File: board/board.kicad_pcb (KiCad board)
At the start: 2 copper layers, 31 parts, among them J1 Screw_Terminal_01x02, J2 Screw_Terminal_01x02, Q1 NPN, Q2 NPN, Q3 NPN

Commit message: Updates PCB file
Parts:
- added J3: Screw_Terminal_01x02, TerminalBlock_4Ucon:TerminalBlock_4Ucon_1x02_P3.50mm_Horizontal, F.Cu at (138.7, 132.1)
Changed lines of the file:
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@@
   (net 16 "Net-(Q2-E)")
   (net 17 "Net-(Q3-C)")
+  (footprint "TerminalBlock_4Ucon:TerminalBlock_4Ucon_1x02_P3.50mm_Horizontal" (layer "F.Cu")
+    (at 138.74 132.08)
+    (descr "Terminal Block 4Ucon ItemNo. 19963, 2 pins, pitch 3.5mm, size 7.7x7mm^2, drill diamater 1.2mm, pad diameter 2.4mm, see http://www.4uconnector.com/online/object/4udrawing/19963.pdf, script-generated using https://github.com/pointhi/kicad-footprint-generator/scripts/TerminalBlock_4Ucon")
+    (tags "THT Terminal Block 4Ucon ItemNo. 19963 pitch 3.5mm size 7.7x7mm^2 drill 1.2mm pad 2.4mm")
+    (property "Sheetfile" "board.kicad_sch")
+    (property "Sheetname" "")
+    (property "ki_description" "Generic screw terminal, single row, 01x02, script generated (kicad-library-utils/schlib/autogen/connector/)")
+    (property "ki_keywords" "screw terminal")
+    (attr through_hole)
+    (fp_text reference "J3" (at 1.75 -4.46) (layer "F.SilkS")
+        (effects (font (size 1 1) (thickness 0.15)))
+    )
+    (fp_text value "Screw_Terminal_01x02" (at 1.75 4.66) (layer "F.Fab")
+        (effects (font (size 1 1) (thickness 0.15)))
+    )
+    (fp_text user "${REFERENCE}" (at 1.75 2.9) (layer "F.Fab")
+        (effects (font (size 1 1) (thickness 0.15)))
+    )
+    (fp_line (start -2.4 2.16) (end -2.4 3.9)
+      (stroke (width 0.12) (type solid)) (layer "F.SilkS"))
+    (fp_line (start -2.4 3.9) (end -0.9 3.9)
+      (stroke (width 0.12) (type solid)) (layer "F.SilkS"))
+    (fp_line (start -2.16 -3.46) (end -2.16 3.66)
+      (stroke (width 0.12) (type solid)) (layer "F.SilkS"))
+    (fp_line (start -2.16 -3.46) (end 5.66 -3.46)
+      (stroke (width 0.12) (type solid)) (layer "F.SilkS"))
+    (fp_line (start -2.16 2.1) (end 5.66 2.1)
+      (stroke (width 0.12) (type solid)) (layer "F.SilkS"))
+    (fp_line (start -2.16 3.66) (end 5.66 3.66)
+      (stroke (width 0.12) (type solid)) (layer "F.SilkS"))
+    (fp_line (start 5.66 -3.46) (end 5.66 3.66)
+      (stroke (width 0.12) (type solid)) (layer "F.SilkS"))
+    (fp_arc (start -1.432109 0.607742) (mid -1.555727 -0.00014) (end -1.432 -0.608)
+      (stroke (width 0.12) (type solid)) (layer "F.SilkS"))
+    (fp_arc (start -0.607742 -1.432109) (mid 0.00014 -1.555727) (end 0.608 -1.432)
+      (stroke (width 0.12) (type solid)) (layer "F.SilkS"))
+    (fp_arc (start 0.027011 1.555493) (mid -0.296984 1.527118) (end -0.608 1.432)
+      (stroke (width 0.12) (type solid)) (layer "F.SilkS"))
+    (fp_arc (start 0.607587 1.431385) (mid 0.310017 1.523783) (end 0 1.555)
+      (stroke (width 0.12) (type solid)) (layer "F.SilkS"))
+    (fp_arc (start 1.432109 -0.607742) (mid 1.555727 0.00014) (end 1.432 0.608)
+      (stroke (width 0.12) (type solid)) (layer "F.SilkS"))
+    (fp_circle (center 3.5 0) (end 5.055 0)
+      (stroke (width 0.12) (type solid)) (fill none) (layer "F.SilkS"))
+    (fp_line (start -2.6 -3.9) (end -2.6 4.1)
+      (stroke (width 0.05) (type solid)) (layer "F.CrtYd"))
+    (fp_line (start -2.6 4.1) (end 6.1 4.1)
+      (stroke (width 0.05) (type solid)) (layer "F.CrtYd"))
+    (fp_line (start 6.1 -3.9) (end -2.6 -3.9)
+      (stroke (width 0.05) (type solid)) (layer "F.CrtYd"))
+    (fp_line (start 6.1 4.1) (end 6.1 -3.9)
+      (stroke (width 0.05) (type solid)) (layer "F.CrtYd"))
+    (fp_line (start -2.1 -3.4) (end 5.6 -3.4)
+      (stroke (width 0.1) (type solid)) (layer "F.Fab"))
+    (fp_line (start -2.1 2.1) (end -2.1 -3.4)
+      (stroke (width 0.1) (type solid)) (layer "F.Fab"))
+    (fp_line (start -2.1 2.1) (end 5.6 2.1)
+      (stroke (width 0.1) (type solid)) (layer "F.Fab"))
+    (fp_line (start -1.1 -0.069) (end -0.069 -0.069)
+      (stroke (width 0.1) (type solid)) (layer "F.Fab"))
+    (fp_line (start -1.1 0.069) (end -1.1 -0.069)
+      (stroke (width 0.1) (type solid)) (layer "F.Fab"))
+    (fp_line (start -0.6 3.6) (end -2.1 2.1)
+      (stroke (width 0.1) (type solid)) (layer "F.Fab"))
+    (fp_line (start -0.069 -1.1) (end 0.069 -1.1)
+      (stroke (width 0.1) (type solid)) (layer "F.Fab"))
+    (fp_line (start -0.069 -0.069) (end -0.069 -1.1)
+      (stroke (width 0.1) (type solid)) (layer "F.Fab"))
+    (fp_line (start -0.069 0.069) (end -1.1 0.069)
+      (stroke (width 0.1) (type solid)) (layer "F.Fab"))
+    (fp_line (start -0.069 1.1) (end -0.069 0.069)
+      (stroke (width 0.1) (type solid)) (layer "F.Fab"))
+    (fp_line (start 0.069 -1.1) (end 0.069 -0.069)
+      (stroke (width 0.1) (type solid)) (layer "F.Fab"))
+    (fp_line (start 0.069 -0.069) (end 1.1 -0.069)
+      (stroke (width 0.1) (type solid)) (layer "F.Fab"))
+    (fp_line (start 0.069 0.069) (end 0.069 1.1)
+      (stroke (width 0.1) (type solid)) (layer "F.Fab"))
+    (fp_line (start 0.069 1.1) (end -0.069 1.1)
+      (stroke (width 0.1) (type solid)) (layer "F.Fab"))
+    (fp_line (start 1.1 -0.069) (end 1.1 0.069)
+      (stroke (width 0.1) (type solid)) (layer "F.Fab"))
+    (fp_line (start 1.1 0.069) (end 0.069 0.069)
+      (stroke (width 0.1) (type solid)) (layer "F.Fab"))
+    (fp_line (start 2.4 -0.069) (end 3.431 -0.069)
+      (stroke (width 0.1) (type solid)) (layer "F.Fab"))
+    (fp_line (start 2.4 0.069) (end 2.4 -0.069)
+      (stroke (width 0.1) (type solid)) (layer "F.Fab"))
+    (fp_line (start 3.431 -1.1) (end 3.569 -1.1)
+      (stroke (width 0.1) (type solid)) (layer "F.Fab"))
+    (fp_line (start 3.431 -0.069) (end 3.431 -1.1)
+      (stroke (width 0.1) (type solid)) (layer "F.Fab"))
+    (fp_line (start 3.431 0.069) (end 2.4 0.069)
+      (stroke (width 0.1) (type solid)) (layer "F.Fab"))
+    (fp_line (start 3.431 1.1) (end 3.431 0.069)
+      (stroke (width 0.1) (type solid)) (layer "F.Fab"))
+    (fp_line (start 3.569 -1.1) (end 3.569 -0.069)
+      (stroke (width 0.1) (type solid)) (layer "F.Fab"))
+    (fp_line (start 3.569 -0.069) (end 4.6 -0.069)
+      (stroke (width 0.1) (type solid)) (layer "F.Fab"))
+    (fp_line (start 3.569 0.069) (end 3.569 1.1)
+      (stroke (width 0.1) (type solid)) (layer "F.Fab"))
+    (fp_line (start 3.569 1.1) (end 3.431 1.1)
+      (stroke (width 0.1) (type solid)) (layer "F.Fab"))
+    (fp_line (start 4.6 -0.069) (end 4.6 0.069)
+      (stroke (width 0.1) (type solid)) (layer "F.Fab"))
+    (fp_line (start 4.6 0.069) (end 3.569 0.069)
+      (stroke (width 0.1) (type solid)) (layer "F.Fab"))
+    (fp_line (start 5.6 -3.4) (end 5.6 3.6)
+      (stroke (width 0.1) (type solid)) (layer "F.Fab"))
+    (fp_line (start 5.6 3.6) (end -0.6 3.6)
+      (stroke (width 0.1) (type solid)) (layer "F.Fab"))
+    (fp_circle (center 0 0) (end 1.375 0)
+      (stroke (width 0.1) (type solid)) (fill none) (layer "F.Fab"))
+    (fp_circle (center 3.5 0) (end 4.875 0)
+      (stroke (width 0.1) (type solid)) (fill none) (layer "F.Fab"))
+    (pad "1" thru_hole rect (at 0 0) (size 2.4 2.4) (drill 1.2) (layers "*.Cu" "*.Mask")
+      (net 13 "9V") (pinfunction "Pin_1") (pintype "passive"))
+    (pad "2" thru_hole circle (at 3.5 0) (size 2.4 2.4) (drill 1.2) (layers "*.Cu" "*.Mask")
+      (net 3 "GND") (pinfunction "Pin_2") (pintype "passive"))
+    (model "${KICAD6_3DMODEL_DIR}/TerminalBlock_4Ucon.3dshapes/TerminalBlock_4Ucon_1x02_P3.50mm_Horizontal.wrl"
+      (offset (xyz 0 0 0))
+      (scale (xyz 1 1 1))
+      (rotate (xyz 0 0 0))
+    )
+  )
   (footprint "Package_TO_SOT_THT:TO-92" (layer "F.Cu")
     (at 102.62 130.58)

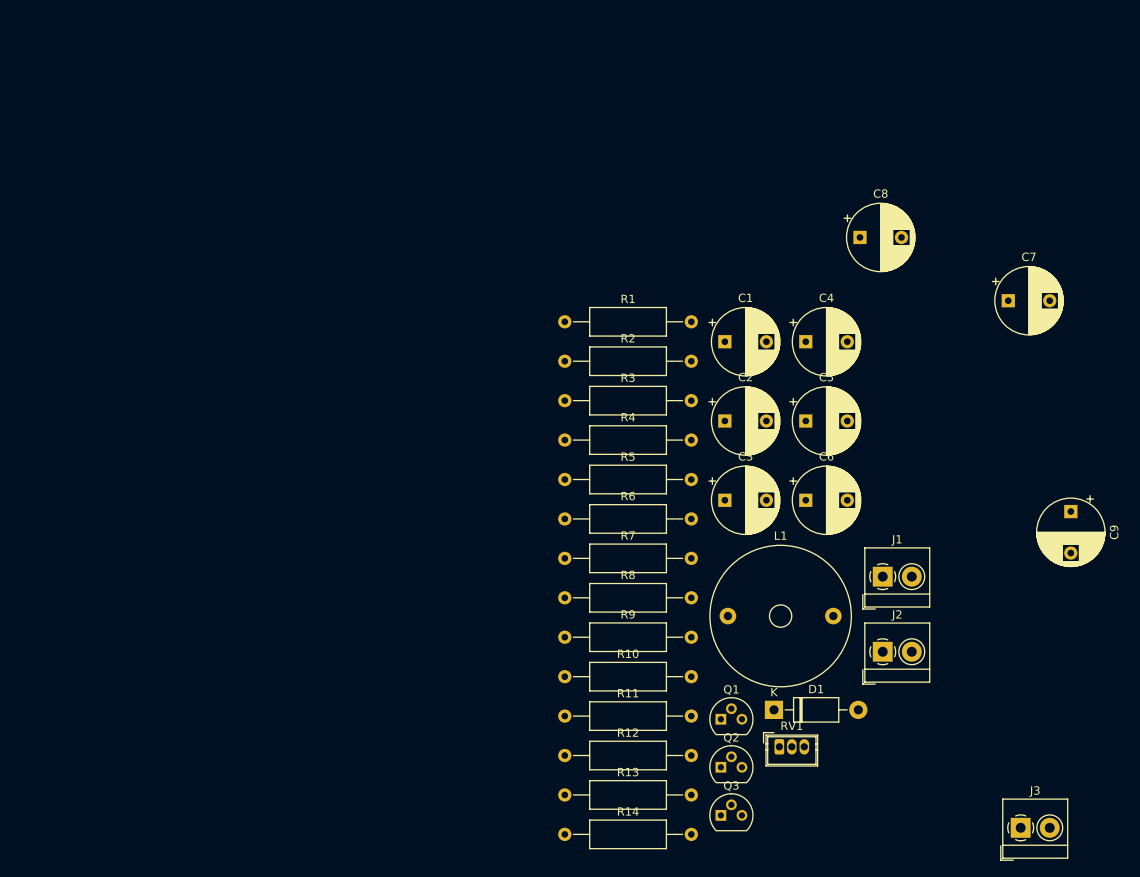
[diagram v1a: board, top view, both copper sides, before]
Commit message: Completed board layout
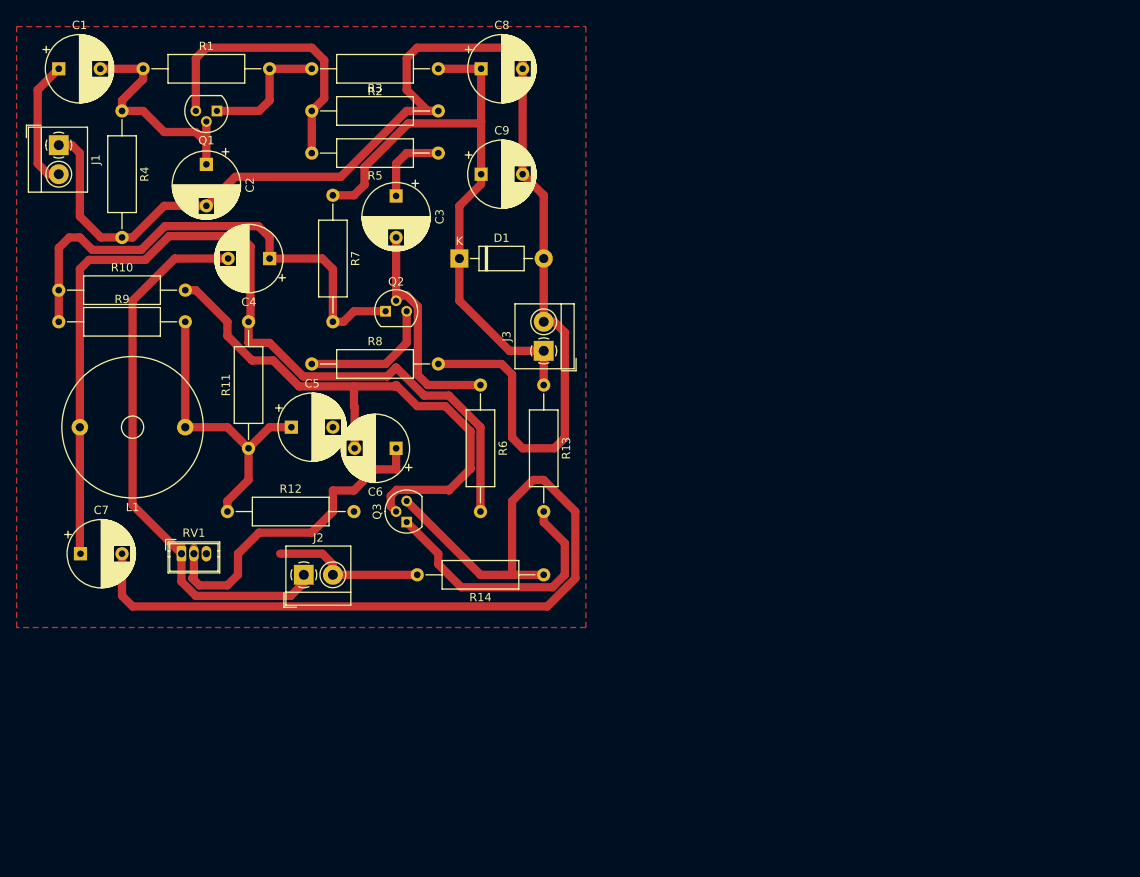
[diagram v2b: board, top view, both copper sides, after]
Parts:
- moved C7 115.8 mm to (25.5, 99.1)
- moved J1 112.0 mm to (22.9, 49.8), turned to -90 degrees
- moved Q1 95.2 mm to (41.9, 45.7), turned to 180 degrees
- moved C1 86.7 mm to (22.9, 40.6)
- moved C9 81.8 mm to (73.7, 53.3), turned to 0 degrees
- moved J3 81.3 mm to (81.3, 74.6), turned to 90 degrees
- moved R10 76.7 mm to (22.9, 67.3)
- moved RV1 75.7 mm to (37.6, 99.1)
- moved R9 71.8 mm to (22.9, 71.1)
- moved J2 70.4 mm to (52.4, 101.6)
- moved C2 69.7 mm to (40.6, 52.1), turned to -90 degrees
- moved L1 69.2 mm to (38.1, 83.8), turned to 180 degrees
- moved Q2 68.2 mm to (62.2, 69.8)
- moved R4 66.5 mm to (30.5, 45.7), turned to -90 degrees
- moved D1 66.3 mm to (71.1, 63.5)
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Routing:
- net GND: track 0.00 -> 176.1 mm, vias 0 -> 1
- net Net-(C7-Pad1): track 0.00 -> 112.0 mm
- net Net-(Q3-E): track 0.00 -> 109.0 mm
- net 9V: track 0.00 -> 73.7 mm
- net Net-(J2-Pin_1): track 0.00 -> 67.8 mm
- net Net-(Q3-B): track 0.00 -> 67.7 mm
- net Net-(Q2-C): track 0.00 -> 61.1 mm
- net Net-(C6-Pad1): track 0.00 -> 39.9 mm
- net Net-(C5-Pad1): track 0.00 -> 36.3 mm
- net Net-(Q1-E): track 0.00 -> 34.8 mm
- net Net-(Q3-C): track 0.00 -> 32.3 mm
- net Net-(Q1-B): track 0.00 -> 28.2 mm
- net Net-(Q2-B): track 0.00 -> 27.4 mm
- net Net-(Q2-E): track 0.00 -> 16.3 mm
- net Net-(Q1-C): track 0.00 -> 15.8 mm
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- added copper zone on F.Cu, net GND
